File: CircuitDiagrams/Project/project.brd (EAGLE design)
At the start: 100 x 70 mm, 124 parts, among them IC1 UC3C, IC2 PCA9542A, IC3 MT48LC4M16A2TSOP54, IC4 TB6593FNGSSOP20, IC5 TB6593FNGSSOP20, J1 JTAG2.54MM2X5TH, J2 1BY2THROUGHHOLE, J3 1BY2THROUGHHOLE, J4 1BY2THROUGHHOLE, J5 8PIN2.54MM2X4TH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

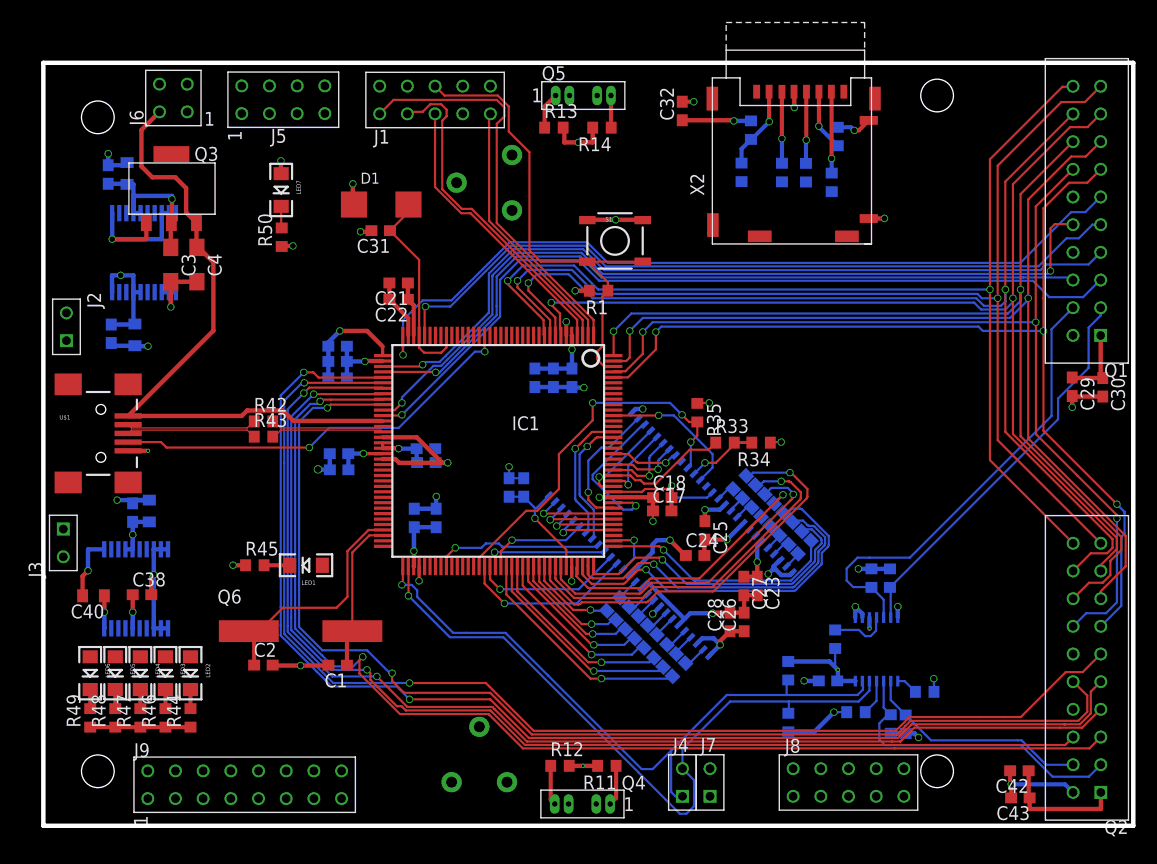
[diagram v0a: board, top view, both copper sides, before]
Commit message: Routed SPI and UART. Added GND to SPI Header
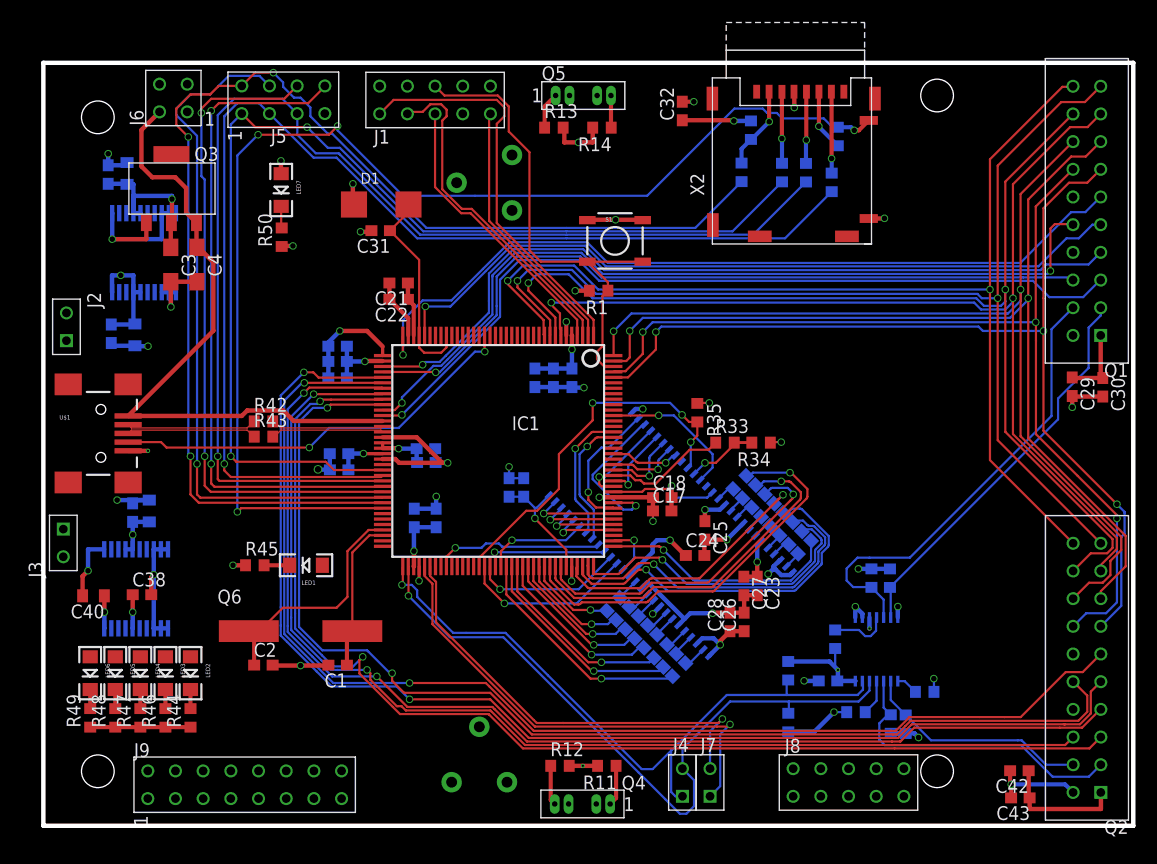
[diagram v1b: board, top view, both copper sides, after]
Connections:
- net GND: now also J5.4
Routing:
- net PB25: track 0.00 -> 115.5 mm, vias 0 -> 3
- net PB21: track 0.00 -> 111.5 mm, vias 0 -> 1
- net PB20: track 0.00 -> 110.5 mm, vias 0 -> 1
- net PB26: track 3.34 -> 112.6 mm, vias 1 -> 4
- net PB19: track 0.00 -> 102.2 mm, vias 0 -> 2
- net PB24: track 0.00 -> 63.5 mm, vias 0 -> 1
- net PB22: track 0.00 -> 61.5 mm, vias 0 -> 2
- net PB23: track 0.00 -> 60.9 mm, vias 0 -> 2
- net PC4: track 0.00 -> 44.2 mm, vias 0 -> 1
- net PC5: track 0.00 -> 40.6 mm, vias 0 -> 1

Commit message: Routed one motor driver and both sensors.
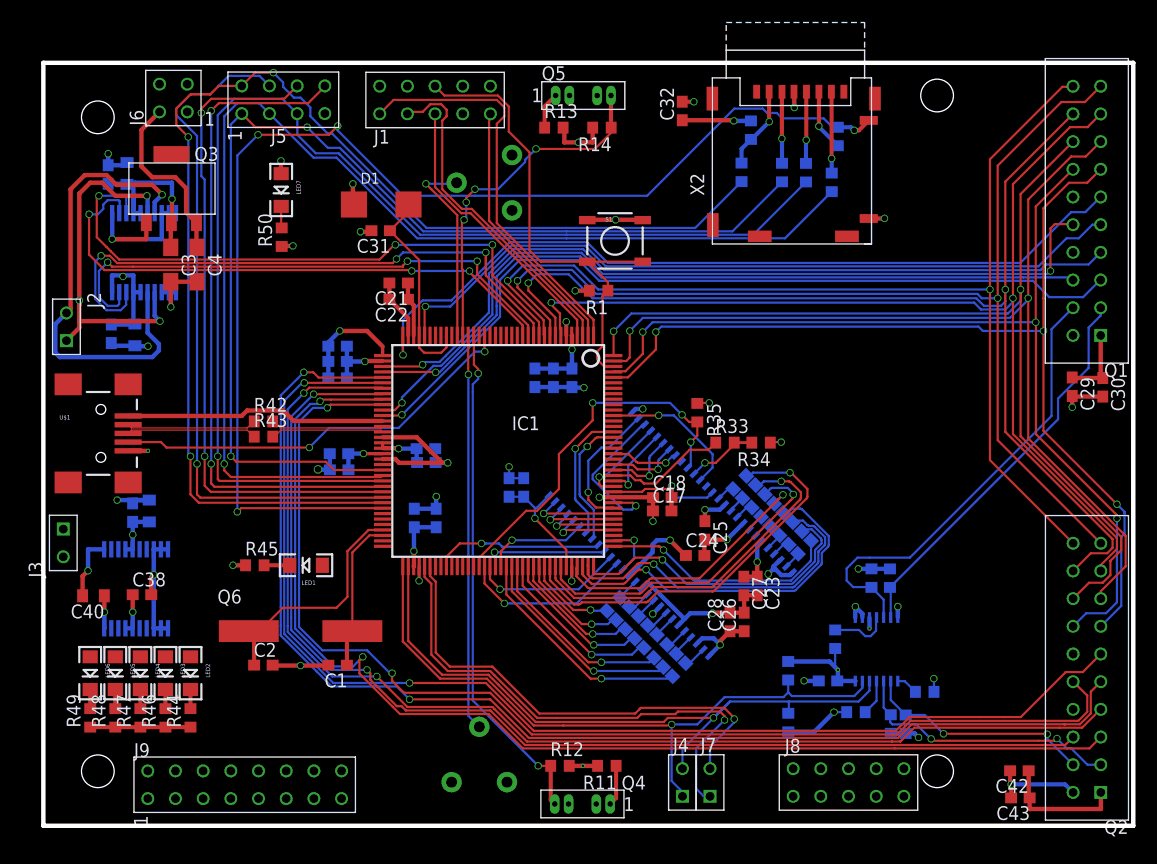
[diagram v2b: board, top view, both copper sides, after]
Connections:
- net N$1 renamed M21
- net N$2 renamed M22
- net N$3 renamed M12
- net N$4 renamed M11
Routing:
- net PB9: track 0.00 -> 56.3 mm, vias 0 -> 3
- net PB8: track 0.00 -> 55.7 mm, vias 0 -> 3
- net PB11: track 0.00 -> 52.2 mm, vias 0 -> 3
- net PB10: track 0.00 -> 50.0 mm, vias 0 -> 3
- net PA6: track 3.65 -> 47.2 mm, vias 0 -> 2
- net M12: track 0.00 -> 42.9 mm, vias 0 -> 1
- net PA7: track 0.00 -> 36.3 mm, vias 0 -> 1
- net M11: track 0.00 -> 33.4 mm, vias 0 -> 3
- net PA8: track 2.96 -> 32.2 mm, vias 0 -> 4
- net +5V: track 59.8 -> 40.6 mm
- net PA9: track 0.00 -> 18.0 mm, vias 0 -> 1
- net PC5: track 40.6 -> 44.0 mm
- net SCL1: track 28.4 -> 25.2 mm, vias 0 -> 2
- net PC4: track 44.2 -> 47.4 mm
- net +3V3: track 172.5 -> 174.5 mm
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
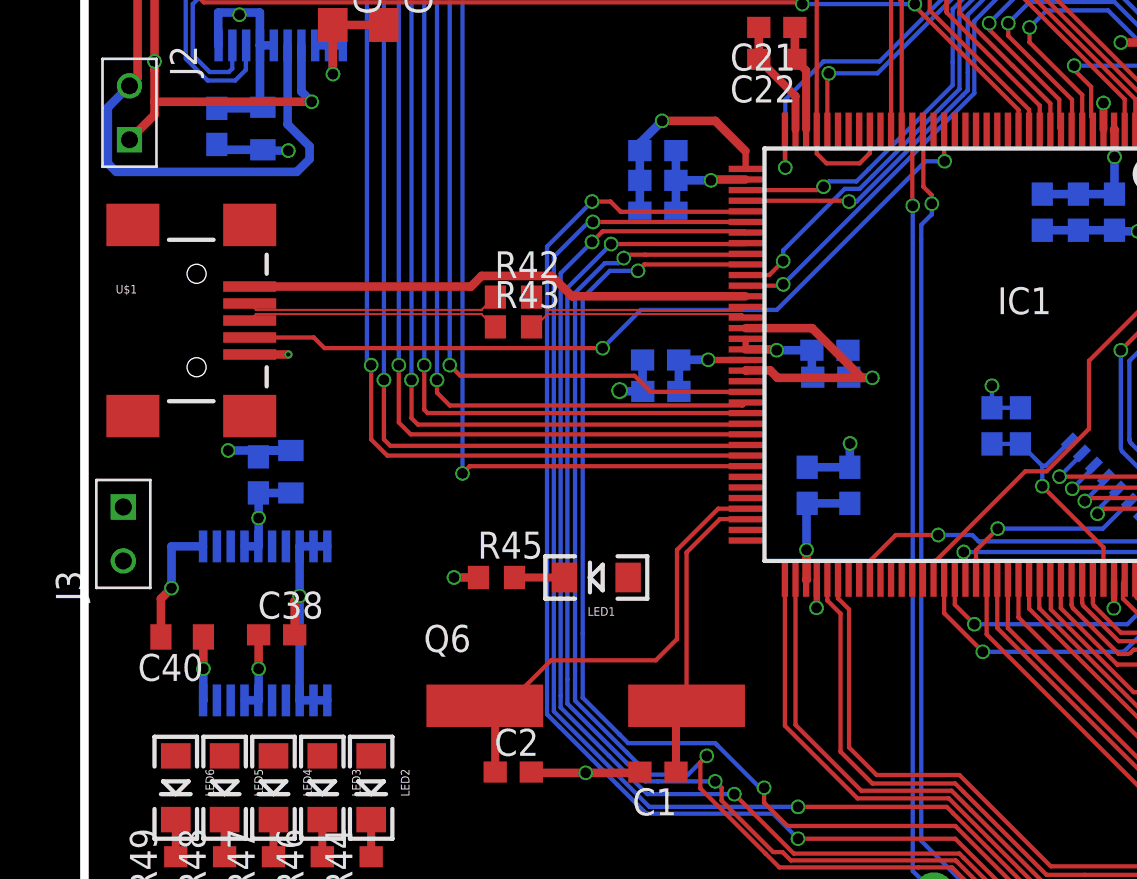
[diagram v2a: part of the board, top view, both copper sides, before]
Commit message: Routed Motor LED and other motor driver
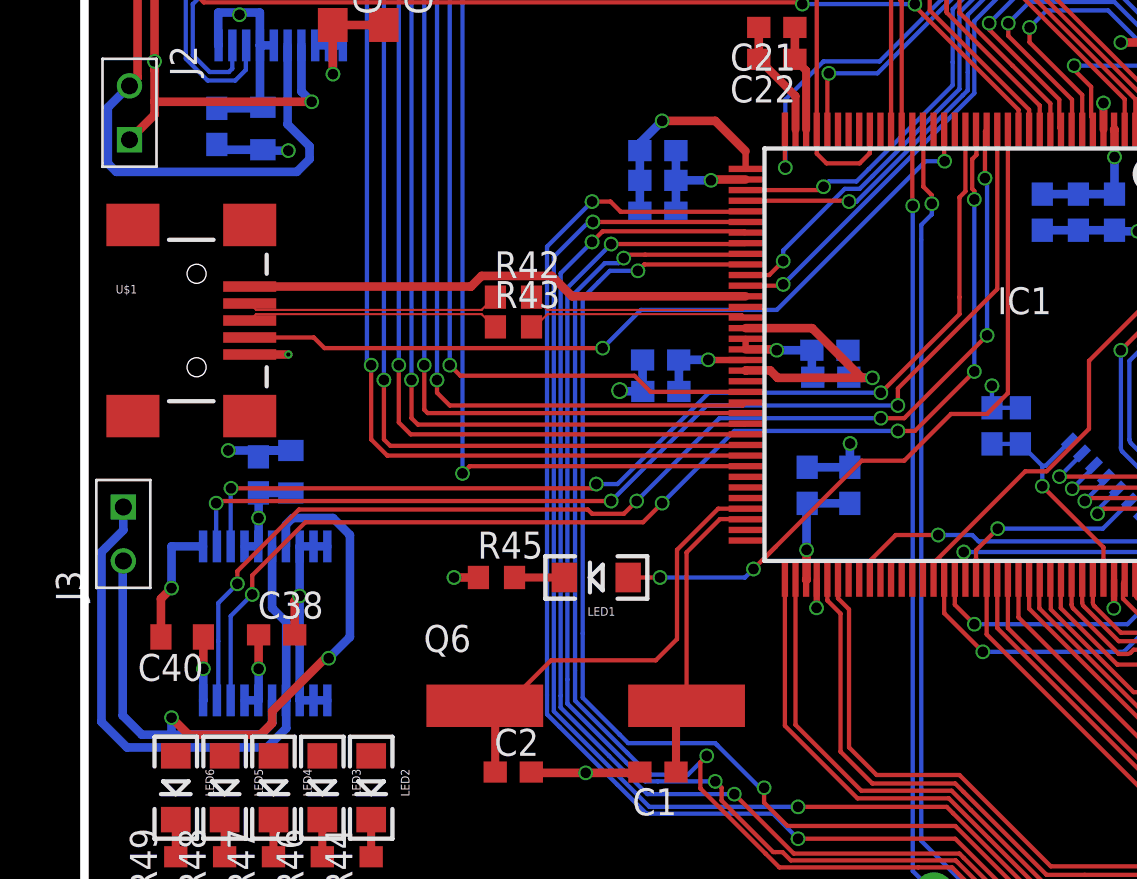
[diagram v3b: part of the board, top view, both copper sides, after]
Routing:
- net PB14: track 0.00 -> 56.3 mm, vias 0 -> 5
- net PB15: track 0.00 -> 55.8 mm, vias 0 -> 5
- net PB13: track 0.00 -> 51.0 mm, vias 0 -> 3
- net PB16: track 0.00 -> 49.2 mm, vias 0 -> 3
- net M22: track 0.00 -> 37.1 mm, vias 0 -> 2
- net PB12: track 0.00 -> 34.7 mm, vias 0 -> 2
- net M21: track 0.00 -> 29.0 mm

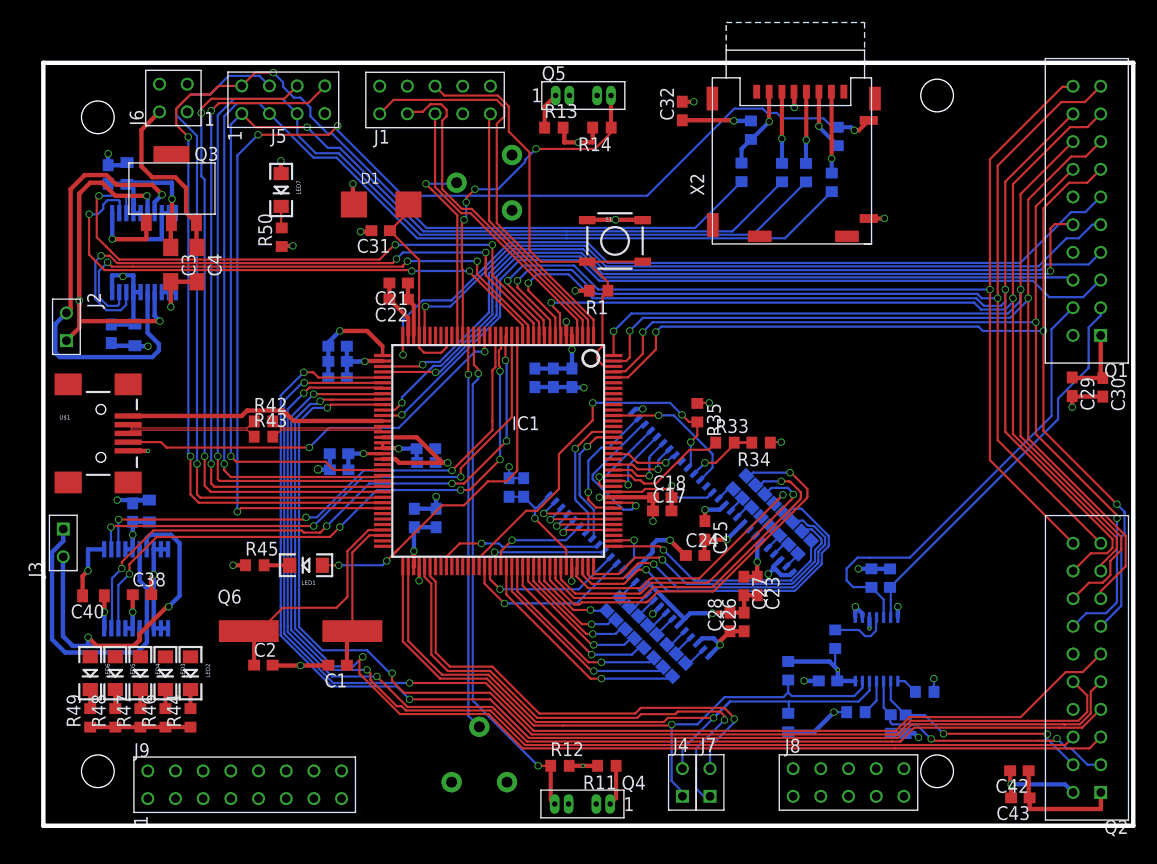
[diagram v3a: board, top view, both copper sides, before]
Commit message: Routed LEDs
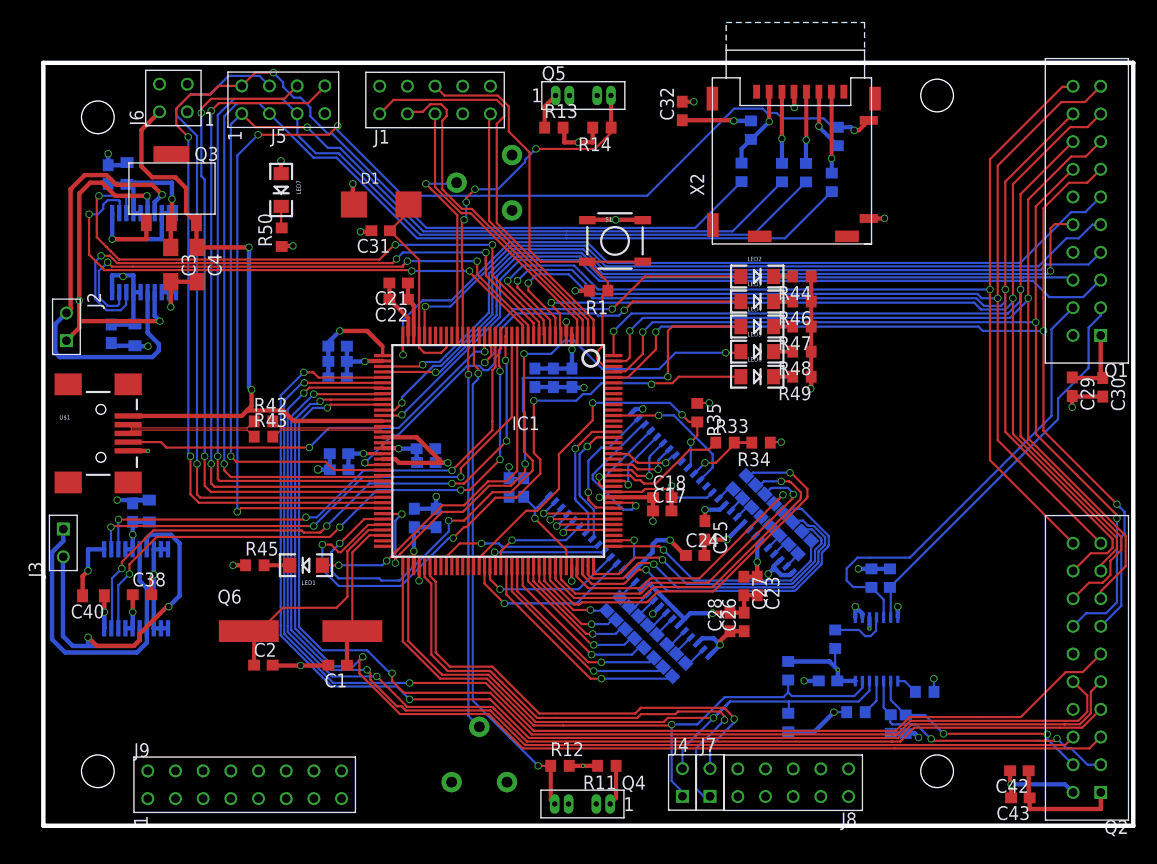
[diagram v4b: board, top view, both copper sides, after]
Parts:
- moved R49 72.4 mm to (69.6, 41.2), turned to 180 degrees
- moved R48 71.4 mm to (69.6, 43.5), turned to 180 degrees
- moved R47 70.5 mm to (69.6, 45.8), turned to 180 degrees
- moved R46 69.8 mm to (69.6, 48.1), turned to 180 degrees
- moved R44 69.2 mm to (69.6, 50.4), turned to 180 degrees
- moved LED6 67.0 mm to (65.5, 41.2), turned to 0 degrees
- moved LED5 65.9 mm to (65.5, 43.5), turned to 0 degrees
- moved LED4 64.9 mm to (65.5, 45.8), turned to 0 degrees
- moved LED3 64.1 mm to (65.5, 48.1), turned to 0 degrees
- moved LED2 63.5 mm to (65.5, 50.4), turned to 0 degrees
- moved J8 5.67 mm to (73.9, 5.22), turned to 180 degrees
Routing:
- net PB28: track 0.00 -> 64.5 mm, vias 0 -> 4
- net PB29: track 0.00 -> 61.0 mm, vias 0 -> 4
- net PB27: track 0.00 -> 55.2 mm, vias 0 -> 4
- net PB18: track 0.00 -> 44.4 mm, vias 0 -> 2
- net PB17: track 0.00 -> 30.8 mm, vias 0 -> 2
- net +5V: track 40.6 -> 60.4 mm, vias 0 -> 2
- net GND: track 183.8 -> 184.9 mm, vias 35 -> 36

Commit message: Revision A of the PCB is done
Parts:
- J8: value 10PIN2.54MM2X5TH -> 6PIN2.54MM2X3TH; device Headers:2.54MM2X5TH -> Headers:2.54MM2X3TH
- moved J8 10.5 mm to (63.7, 2.70), turned to 0 degrees
- moved D1 3.01 mm to (28.0, 56.8)
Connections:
- net PA10: now also J8.3; no longer J8.7
- net PA12: now also J8.4; no longer J8.8
- net PA13: now also J8.5; no longer J8.9
- net PA14: now also J8.6; no longer J8.10
- net PA5: now also J8.2; no longer J8.6
- net PC7: no longer J9.13
- net PD16: no longer J8.2
- net PD18: no longer J8.3
- net PD19: no longer J8.4
- net PD22: no longer J8.5
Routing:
- net PA14: track 0.00 -> 146.9 mm, vias 0 -> 4
- net PA13: track 0.00 -> 143.7 mm, vias 0 -> 3
- net PD23: track 0.00 -> 142.5 mm, vias 0 -> 2
- net PA12: track 0.00 -> 137.8 mm, vias 0 -> 3
- net PD27: track 0.00 -> 134.1 mm, vias 0 -> 2
- net PD28: track 0.00 -> 132.5 mm, vias 0 -> 1
- net PD29: track 0.00 -> 131.2 mm, vias 0 -> 1
- net PD30: track 0.00 -> 130.7 mm, vias 0 -> 1
- net PA10: track 0.00 -> 129.4 mm, vias 0 -> 3
- net PA5: track 0.00 -> 120.6 mm, vias 0 -> 8
- net PD25: track 0.00 -> 81.6 mm, vias 0 -> 3
- net PD4: track 0.00 -> 79.4 mm, vias 0 -> 3
- net PD26: track 0.00 -> 70.8 mm, vias 0 -> 6
- net PC9: track 0.00 -> 49.0 mm, vias 0 -> 5
- net PC11: track 0.00 -> 44.1 mm, vias 0 -> 3
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
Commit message: Sorting Keepout Errors. 96 to go!
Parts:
- moved R42 3.20 mm to (17.0, 37.0)
- moved C23 2.60 mm to (68.1, 22.0)
- moved C21 2.51 mm to (30.3, 48.7), turned to 270 degrees
- moved Q5 1.00 mm to (47.1, 68.0)
- moved C17 0.81 mm to (56.8, 28.1)
- moved C8 0.80 mm to (35.1, 35.4)
- moved C26 0.80 mm to (65.1, 18.7)
- moved C20 0.70 mm to (27.0, 44.7)
- moved C15 0.70 mm to (42.0, 31.0)
- moved C10 0.60 mm to (44.5, 41.1)
- moved C6 0.60 mm to (27.1, 34.7)
- moved C9 0.60 mm to (27.0, 40.5)
- moved C22 0.45 mm to (32.4, 48.7), turned to 270 degrees
- moved C24 0.30 mm to (59.8, 24.5)
- moved R43 0.28 mm to (20.0, 35.9)
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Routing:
- net +5V: track 60.4 -> 48.3 mm
- net GND: track 185.2 -> 194.1 mm
- net +3V3: track 174.5 -> 181.7 mm, vias 32 -> 31
- net USB_N: track 11.9 -> 8.45 mm
- net DATA_N: track 10.4 -> 13.5 mm
- net ADCREFP: track 5.03 -> 7.27 mm
- net PA8: track 33.5 -> 34.6 mm
- net N$6: track 3.37 -> 4.41 mm
- net VDDCORE: track 4.66 -> 5.23 mm
- net USB_P: track 11.9 -> 11.4 mm
